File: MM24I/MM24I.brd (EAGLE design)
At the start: 80.4 x 77 mm, 21 parts, among them IC1 SN74LVC2G17DBVR, IC2 SN74LVC14APWR, U1 SN74LVCH16374ADGGR, U2 SN74LVCH16374ADGGR, U3 CY14B104M, U4 SN74AHCT16373DGGR, X1 FH21-18S-1DSA, X2 FH21-18S-1DSA, X3 FH21-18S-1DSA, X4 FH21-18S-1DSA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

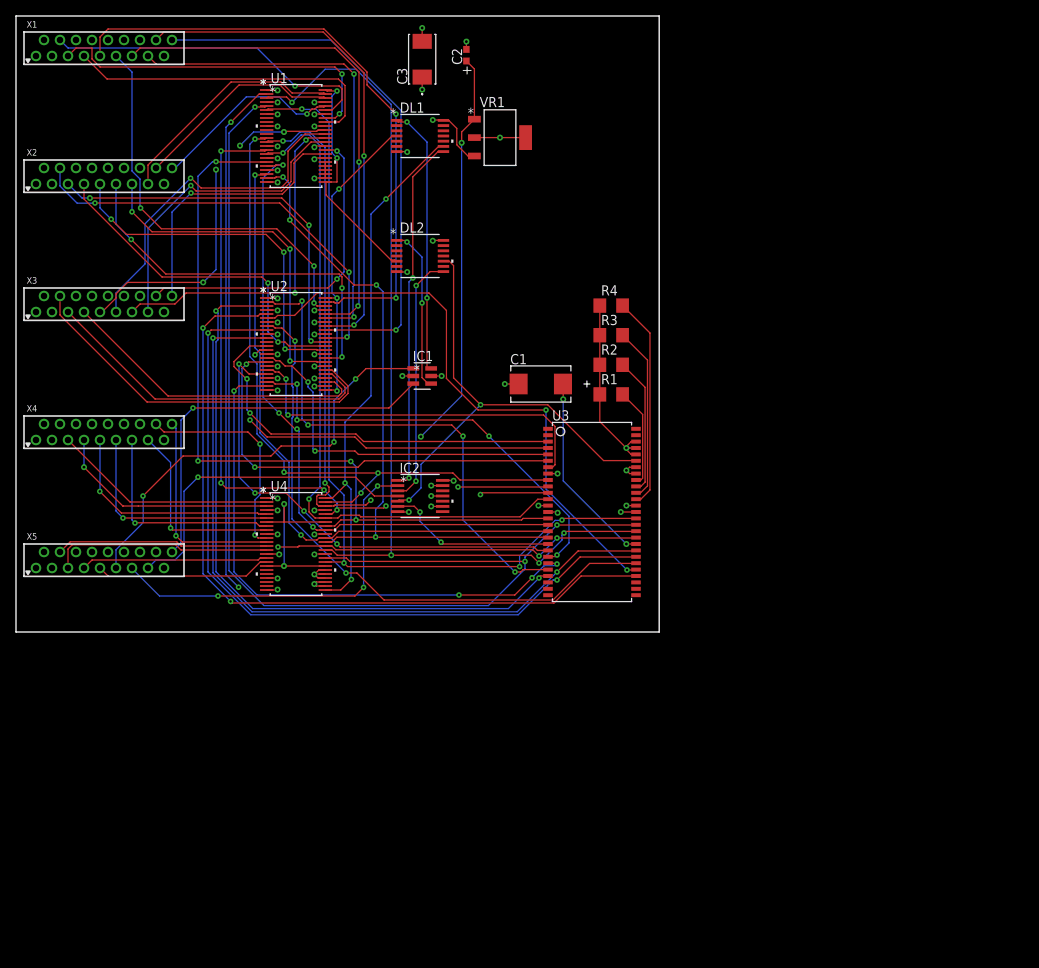
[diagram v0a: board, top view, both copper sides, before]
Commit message: Redesigned memory expansion to fit on a single flip chip, consolidated component libraries, etc.
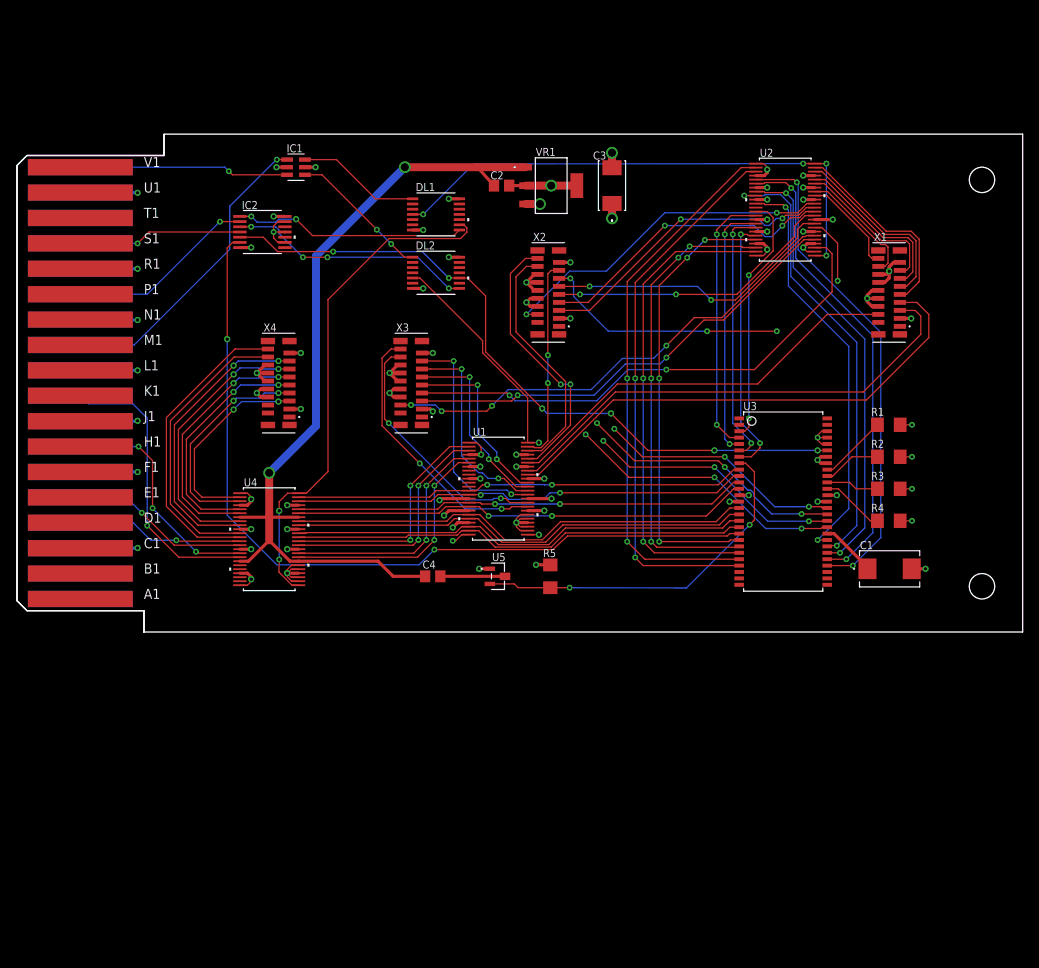
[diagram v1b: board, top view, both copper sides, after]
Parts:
- removed X5: FH21-18S-1DSA, con-hirose:FH21-18S-1DSA
- added C4: 0.1 UF, rcl:C0805
- added R5: 10k, rcl:R1206
- added U$1: SINGLE, dec-con:EDGE-CON2
- added U$2: (no value), dec-con:SINGLE
- added U5: TLV803SDBZ, MM24I:DBZ3
- C1: value 470UF -> 100UF; device AVX_By_element14_Batch_1:CAPCP7343X430N -> MM24I:CAPCP7343X430N
- C2: device MM24I:CC0603N -> rcl:C0805
- X1, X2, X3, X4: value FH21-18S-1DSA -> FH12-18S-0.5SV(55); device con-hirose:FH21-18S-1DSA -> MM24I:CON18_1X18_DUTB_HRS
- moved X1 100.3 mm to (105.0, 38.2), turned to 270 degrees
- moved U2 63.4 mm to (96.0, 52.8)
- moved X2 54.8 mm to (62.4, 38.2), turned to 270 degrees
- moved U1 50.8 mm to (60.2, 17.9)
- moved C1 49.3 mm to (109.1, 7.90), turned to 0 degrees
- moved R4 43.9 mm to (109.0, 13.9), turned to 180 degrees
- moved R3 39.7 mm to (109.0, 17.9), turned to 180 degrees
- moved IC2 38.4 mm to (30.7, 50.0)
- moved X3 37.2 mm to (45.3, 26.9), turned to 270 degrees
- moved R2 36.6 mm to (109.0, 21.9), turned to 180 degrees
- moved R1 34.9 mm to (109.0, 25.9), turned to 180 degrees
- moved IC1 30.5 mm to (34.9, 58.1)
- moved C3 28.5 mm to (74.4, 55.8)
- moved U3 23.9 mm to (95.8, 16.3)
- moved X4 17.9 mm to (28.7, 26.9), turned to 270 degrees
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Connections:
- net N$1 renamed VCAP
- new net !POWER-OK: R5.2, U3.8, U5.2
- new net N$1: C4.2, U5.3
- net +5V: now also C4.1
- net GND: now also U$1.C2, U$1.F2, U$1.J2, U$1.L2, U$1.N2, U$1.R2, U$1.U2, U5.1; no longer U3.8, X5.10, X5.12, X5.14, X5.17, X5.3, X5.6, X5.8
- net MCS-MEM-08-H: now also U$1.D2; no longer X5.4
- net MCS-MEM-09-H: now also U$1.E2; no longer X5.5
- net MCS-MEM-10-H: now also U$1.H2; no longer X5.7
- net MCS-MEM-11-H: now also U$1.K2; no longer X5.9
- net MCT-MEM-DONE-L: now also U$1.S2; no longer X5.15
- net MCT-STROBE-L: now also U$1.P2; no longer X5.13
- net MXB-MEM-TP3-H: now also U$1.V2; no longer X5.18
- net MXB-START-MEMORY-H: now also U$1.M2; no longer X5.11
- net VCC: now also R5.1
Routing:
- net GND: track 102.5 -> 208.6 mm, vias 48 -> 64
- net !WRITE-ENABLE: track 21.4 -> 103.4 mm
- net MXB-BMA-05-H: track 68.8 -> 12.5 mm, vias 1 -> 0
- net N$16: track 143.7 -> 88.5 mm, vias 3 -> 5
- net MXB-BMA-00-H: track 77.3 -> 25.2 mm, vias 2 -> 0
- net MXB-BMA-04-H: track 64.2 -> 15.4 mm, vias 2 -> 0
- net !POWER-OK: track 0.00 -> 45.1 mm, vias 0 -> 2
- net MXB-BMA-02-H: track 63.8 -> 21.2 mm, vias 2 -> 0
- net N$45: track 94.2 -> 51.6 mm
- net N$6: track 99.9 -> 58.4 mm, vias 4 -> 0
- net MXB-BMA-03-H: track 60.8 -> 19.3 mm, vias 2 -> 0
- net N$44: track 96.1 -> 56.1 mm
- net N$4: track 94.0 -> 56.6 mm, vias 6 -> 2
- net N$41: track 96.4 -> 62.2 mm
- net N$2: track 86.9 -> 56.5 mm, vias 4 -> 2
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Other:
- board size 80.4 x 77 mm -> 125.7 x 62.2 mm

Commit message: Fix typo in , change FFC reference designators to match backplane slot names on MM24I
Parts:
- renumbered X1 to N20, X2 to N21, X3 to N22, X4 to N23

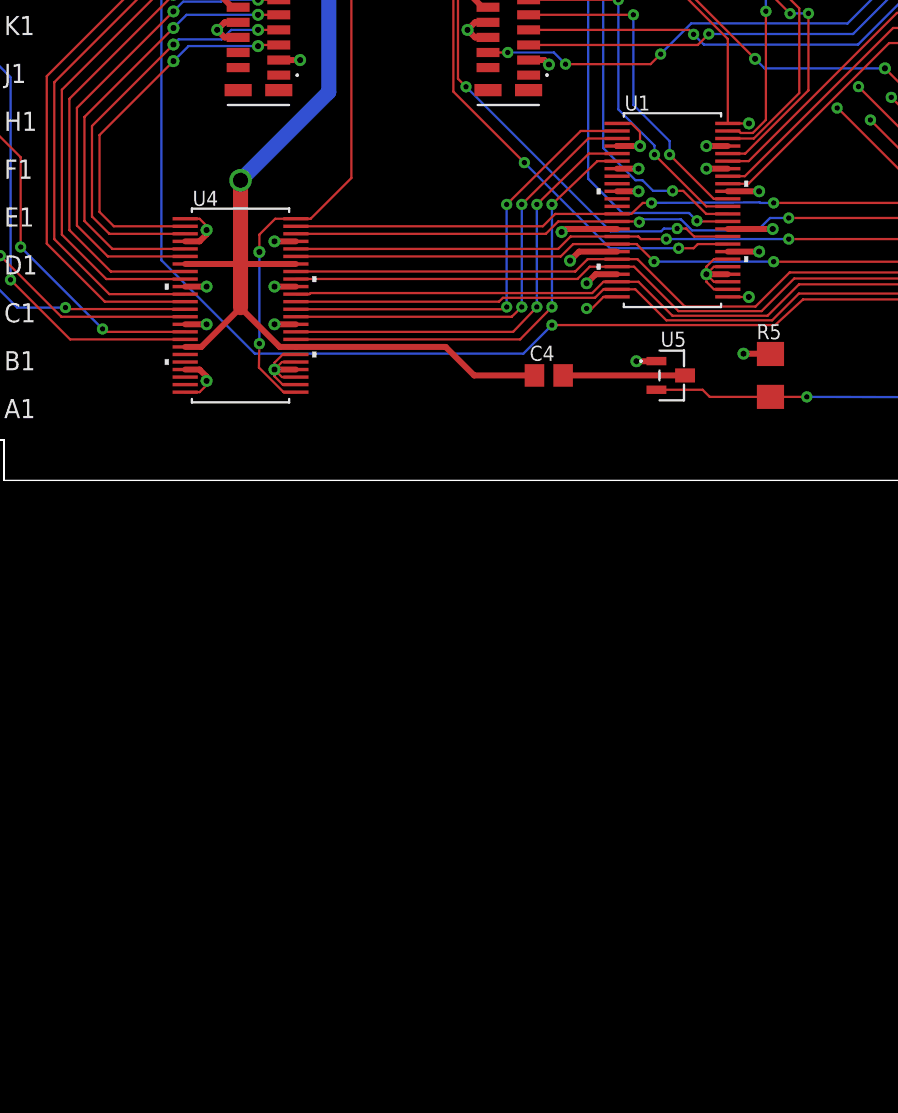
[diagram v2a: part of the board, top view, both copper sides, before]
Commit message: Add bypass capacitors to schematic
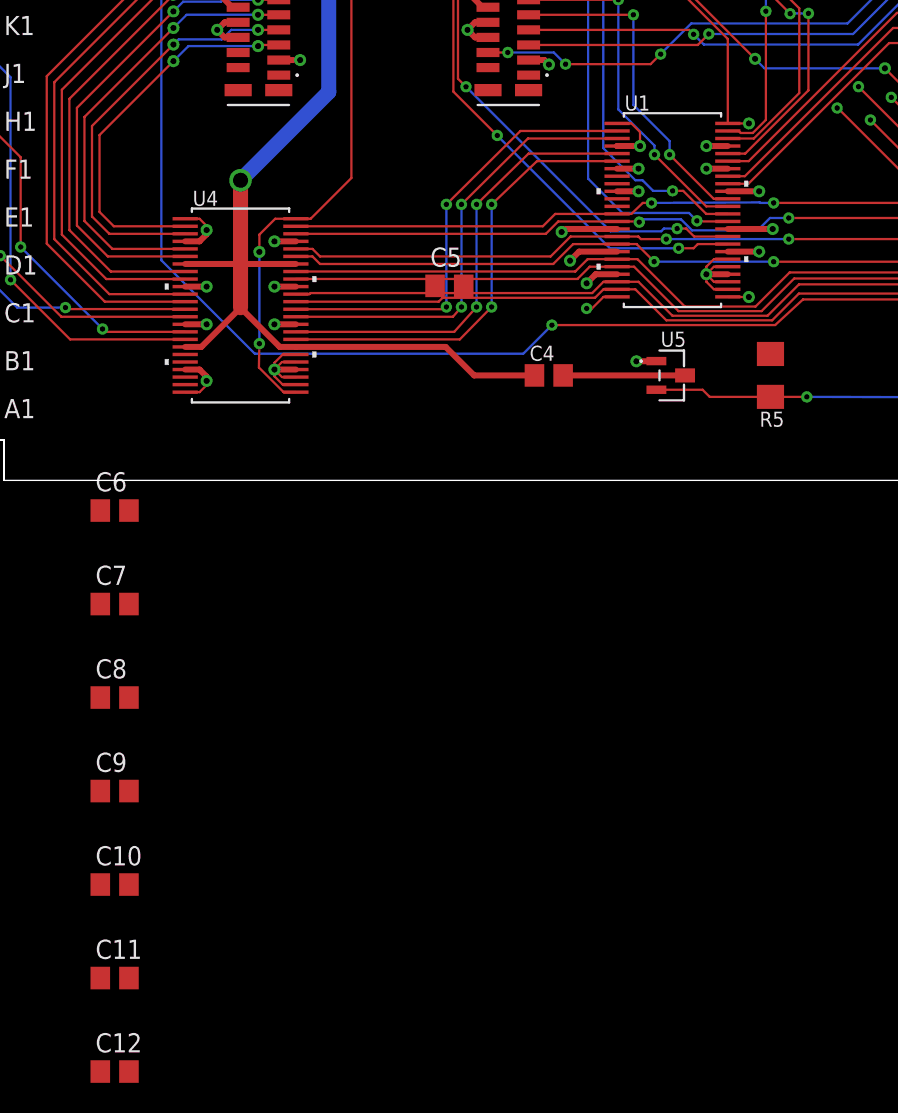
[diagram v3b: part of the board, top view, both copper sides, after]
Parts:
- added C10, C11, C12, C5, C6, C7, C8, C9: 0.1 UF, rcl:C0805
- turned R5 to 90 degrees
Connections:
- net !POWER-OK: now also R5.1; no longer R5.2
- net GND: now also C10.2, C11.2, C12.2, C5.2, C6.2, C7.2, C8.2, C9.2
- net VCC: now also C10.1, C11.1, C12.1, C5.1, C6.1, C7.1, C8.1, C9.1, R5.2; no longer R5.1
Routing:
- net N$14: track 89.9 -> 93.9 mm
- net N$15: track 88.2 -> 92.2 mm
- net N$16: track 88.5 -> 92.5 mm
- net N$17: track 86.3 -> 90.3 mm
- net VCC: track 27.2 -> 25.4 mm, vias 17 -> 16

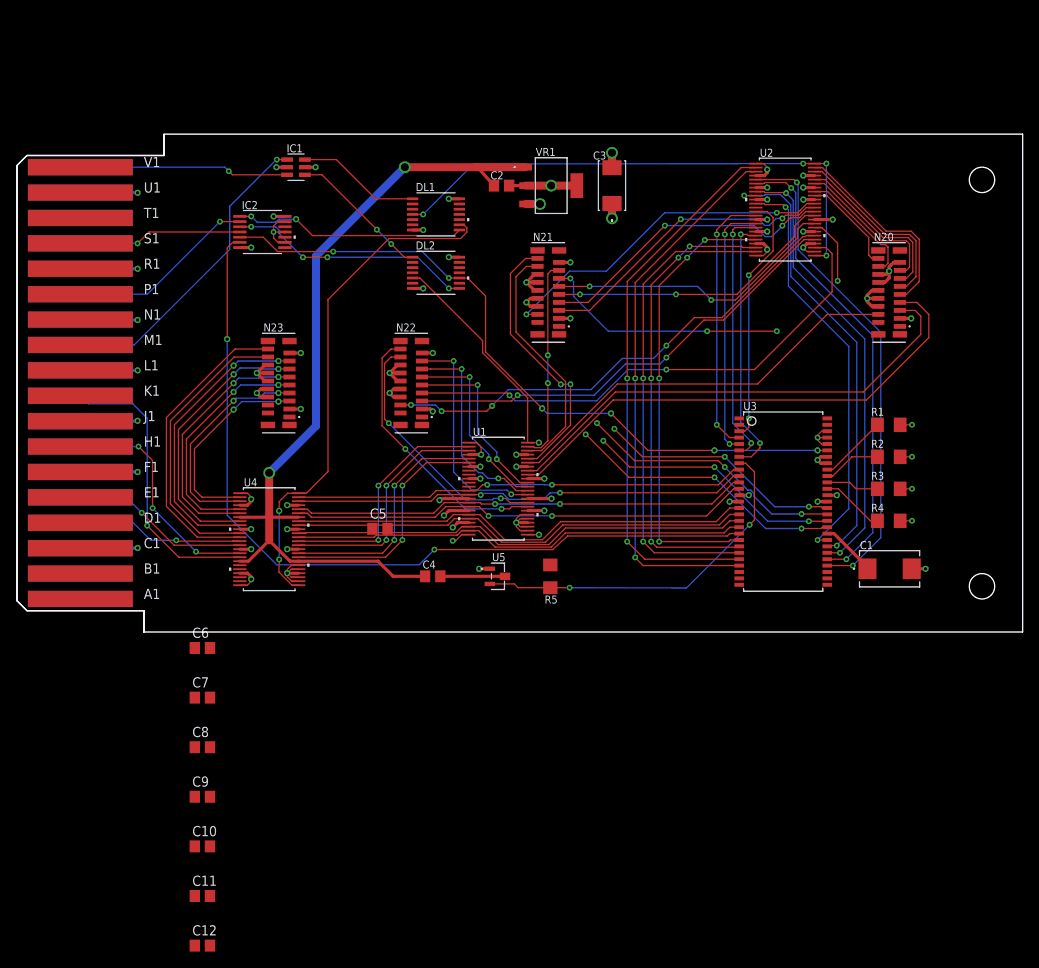
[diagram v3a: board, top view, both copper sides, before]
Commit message: Added bypass capacitors, reworked W021J
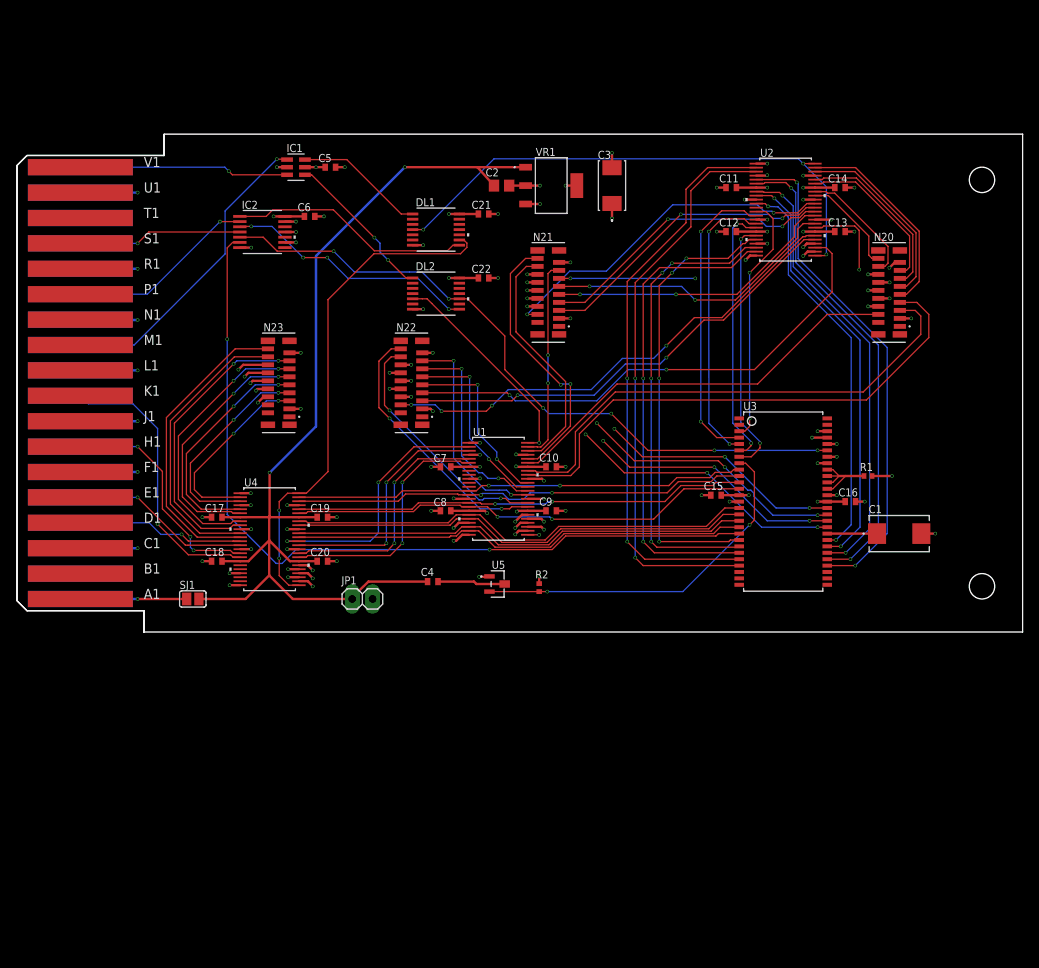
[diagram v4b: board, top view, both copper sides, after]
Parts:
- removed R3, R4, R5: 10k, rcl:R1206
- added C13, C15, C16, C17, C18, C19, C20: 0.01 UF, rcl:C0402
- added C14, C21, C22: 0.1 UF, rcl:C0402
- added JP1: (no value), pinhead:1X02
- added SJ1: (no value), jumper:SJ
- C10, C11, C12, C7, C8, C9: value 0.1 UF -> 0.01 UF; device rcl:C0805 -> rcl:C0402
- C4, C5, C6: device rcl:C0805 -> rcl:C0402
- R1, R2: device rcl:R1206 -> rcl:R0402
- moved C12 111.1 mm to (89.3, 50.0), turned to 180 degrees
- moved C11 110.5 mm to (89.3, 55.5), turned to 180 degrees
- moved C10 64.4 mm to (66.8, 20.6)
- moved C9 56.4 mm to (66.8, 15.2)
- moved C6 55.6 mm to (36.6, 52.0)
- moved R2 46.7 mm to (65.3, 5.55), turned to 90 degrees
- moved C5 45.6 mm to (39.2, 58.1)
- moved C8 42.4 mm to (53.6, 15.2), turned to 180 degrees
- moved C7 41.9 mm to (53.6, 20.6), turned to 180 degrees
- moved R1 6.91 mm to (106.4, 19.5)
- moved C1 4.56 mm to (110.3, 12.3)
- moved DL2 2.60 mm to (52.4, 42.3)
- moved DL1 1.90 mm to (52.4, 50.3)
- moved U5 0.96 mm to (60.1, 6.00)
- moved C4 0.66 mm to (52.0, 6.30)
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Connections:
- removed net N$10: R2.2, U3.45
- removed net N$12: R3.2, U3.44
- removed net N$8: R4.2, U3.43
- new net +5-BACKPLANE: SJ1.1, U$1.A2
- net !POWER-OK: now also R2.1; no longer R5.1
- net +5V: now also C17.1, C18.1, C19.1, C20.1, JP1.1, SJ1.2
- net GND: now also C13.2, C14.2, C15.2, C16.2, C17.2, C18.2, C19.2, C20.2, C21.2, C22.2, JP1.2; no longer R2.1, R3.1, R4.1
- net N$9: now also U3.43, U3.44, U3.45
- net VCC: now also C13.1, C14.1, C15.1, C16.1, C21.1, C22.1, R2.2; no longer R5.2
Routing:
- net VCC: track 25.4 -> 56.7 mm, vias 16 -> 17
- net +5V: track 105.5 -> 134.3 mm
- net +5-BACKPLANE: track 0.00 -> 13.3 mm, vias 0 -> 1
- net N$8: track 7.93 -> 0.00 mm
- net N$10: track 7.27 -> 0.00 mm
- net N$12: track 6.61 -> 0.00 mm
- net N$33: track 33.5 -> 37.6 mm
- net N$31: track 32.4 -> 35.7 mm
- net N$44: track 56.1 -> 53.1 mm
- net N$40: track 68.6 -> 71.3 mm
- net N$9: track 8.60 -> 11.2 mm
- net MXB-MCBMB-04-H: track 61.4 -> 63.9 mm
- net N$30: track 69.4 -> 71.9 mm
- net MXB-MCBMB-05-H: track 64.4 -> 66.9 mm
- net N$14: track 93.9 -> 96.2 mm
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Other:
- board text added: "+5"
- board text added: "GND"
